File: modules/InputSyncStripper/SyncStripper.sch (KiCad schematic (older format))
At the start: 12 parts

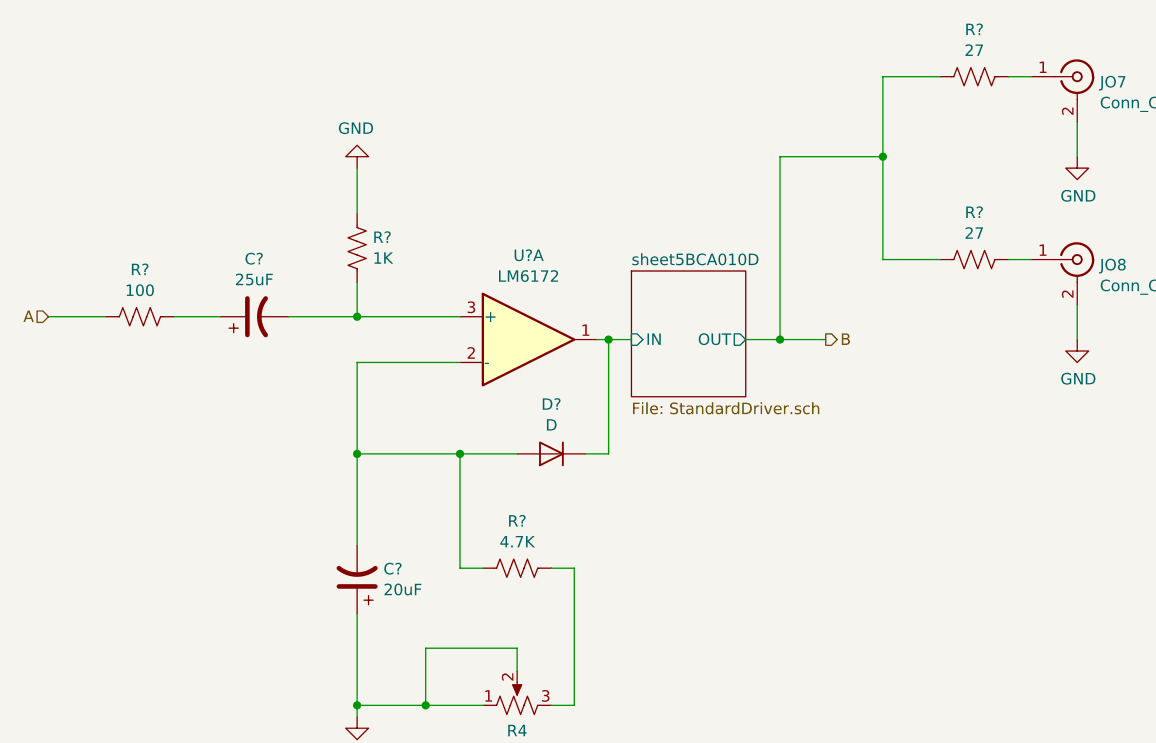
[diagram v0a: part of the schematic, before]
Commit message: fix some ERC issues; assign symbols
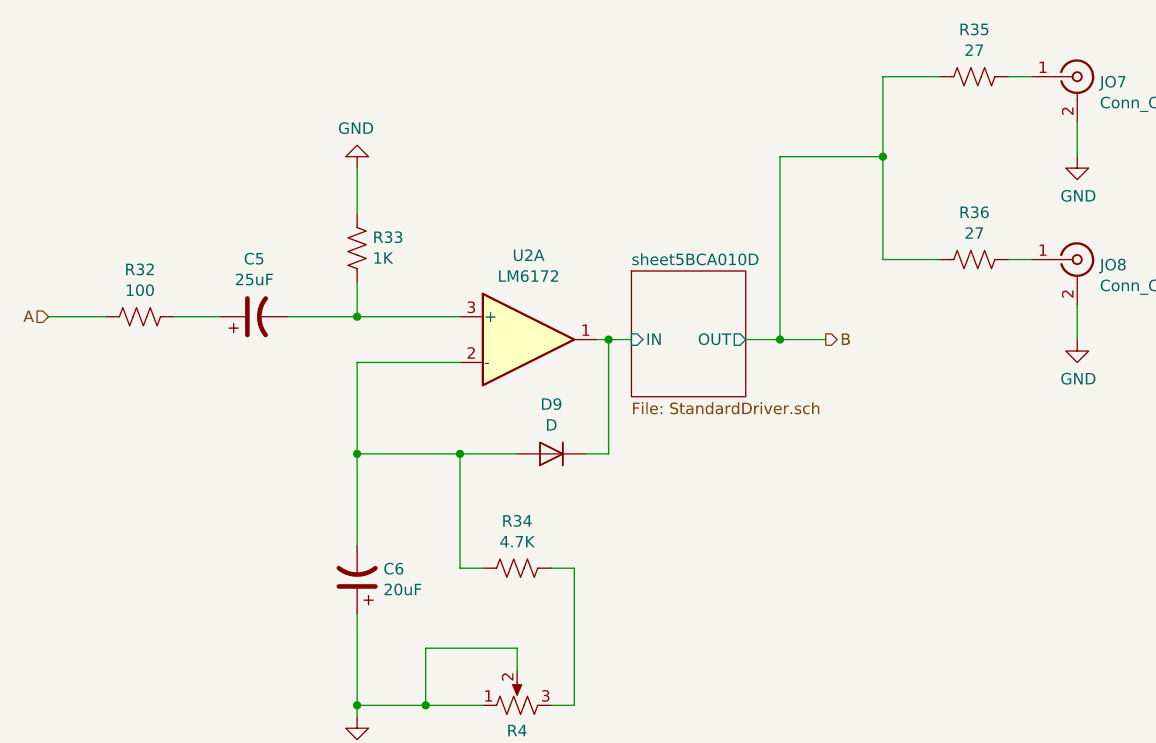
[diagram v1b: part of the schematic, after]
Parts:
- gave numbers to parts that had none: 9
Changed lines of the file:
@@
 EESchema Schematic File Version 4
-LIBS:SIP-cache
+LIBS:InputSyncStripper-cache
 EELAYER 26 0
 EELAYER END
@@
 B
 $Comp
-L Amplifier_Operational:LM6172 U?
+L Amplifier_Operational:LM6172 U2
 U 1 1 5BCA5CA5
 P 4550 3600
-F 0 "U?" H 4550 3967 50  0000 C CNN
+F 0 "U2" H 4550 3967 50  0000 C CNN
 F 1 "LM6172" H 4550 3876 50  0000 C CNN
 F 2 "" H 4550 3600 50  0001 C CNN
@@
 $EndComp
 $Comp
-L Device:R_US R?
+L Device:R_US R35
 U 1 1 5BCA026E
 P 6500 2450
-F 0 "R?" V 6295 2450 50  0000 C CNN
+F 0 "R35" V 6295 2450 50  0000 C CNN
 F 1 "27" V 6386 2450 50  0000 C CNN
 F 2 "" V 6540 2440 50  0001 C CNN
@@
 $EndComp
 $Comp
-L power:GND #PWR?
+L power:GND #PWR016
 U 1 1 5BCA04DE
 P 6950 2800
-F 0 "#PWR?" H 6950 2550 50  0001 C CNN
+F 0 "#PWR016" H 6950 2550 50  0001 C CNN
 F 1 "GND" H 6955 2627 50  0000 C CNN
 F 2 "" H 6950 2800 50  0001 C CNN
@@
 $EndComp
 $Comp
-L Device:R_US R?
+L Device:R_US R36
 U 1 1 5BCA0768
 P 6500 3250
-F 0 "R?" V 6295 3250 50  0000 C CNN
+F 0 "R36" V 6295 3250 50  0000 C CNN
 F 1 "27" V 6386 3250 50  0000 C CNN
 F 2 "" V 6540 3240 50  0001 C CNN
@@
 $EndComp
 $Comp
-L power:GND #PWR?
+L power:GND #PWR017
 U 1 1 5BCA076E
 P 6950 3600
-F 0 "#PWR?" H 6950 3350 50  0001 C CNN
+F 0 "#PWR017" H 6950 3350 50  0001 C CNN
 F 1 "GND" H 6955 3427 50  0000 C CNN
 F 2 "" H 6950 3600 50  0001 C CNN
@@
 $EndComp
 $Comp
-L Device:CP1 C?
+L Device:CP1 C6
 U 1 1 5BCA0CB3
 P 3800 4650
-F 0 "C?" H 3685 4604 50  0000 R CNN
+F 0 "C6" H 3685 4604 50  0000 R CNN
 F 1 "20uF" H 3685 4695 50  0000 R CNN
 F 2 "" H 3800 4650 50  0001 C CNN
@@
 $EndComp
 $Comp
-L Device:D D?
+L Device:D D9
 U 1 1 5BCA0DC4
 P 4650 4100
-F 0 "D?" H 4650 3884 50  0000 C CNN
+F 0 "D9" H 4650 3884 50  0000 C CNN
 F 1 "D" H 4650 3975 50  0000 C CNN
 F 2 "" H 4650 4100 50  0001 C CNN
@@
 	4900 3600 5000 3600
 $Comp
-L power:GND #PWR?
+L power:GND #PWR015
 U 1 1 5BCA11AF
 P 3800 5250
-F 0 "#PWR?" H 3800 5000 50  0001 C CNN
+F 0 "#PWR015" H 3800 5000 50  0001 C CNN
 F 1 "GND" H 3805 5077 50  0000 C CNN
 F 2 "" H 3800 5250 50  0001 C CNN
@@
 $EndComp
 $Comp
-L Device:R_US R?
+L Device:R_US R34
 U 1 1 5BCA123D
 P 4500 4600
-F 0 "R?" V 4295 4600 50  0000 C CNN
+F 0 "R34" V 4295 4600 50  0000 C CNN
 F 1 "4.7K" V 4386 4600 50  0000 C CNN
 F 2 "" V 4540 4590 50  0001 C CNN
@@
 	4100 5200 3800 5200
 $Comp
-L Device:CP1 C?
+L Device:CP1 C5
 U 1 1 5BCA29B1
 P 3350 3500
-F 0 "C?" V 3602 3500 50  0000 C CNN
+F 0 "C5" V 3602 3500 50  0000 C CNN
 F 1 "25uF" V 3511 3500 50  0000 C CNN
 F 2 "" H 3350 3500 50  0001 C CNN
@@
 $EndComp
 $Comp
-L Device:R_US R?
+L Device:R_US R32
 U 1 1 5BCA2A51
 P 2850 3500
-F 0 "R?" V 2645 3500 50  0000 C CNN
+F 0 "R32" V 2645 3500 50  0000 C CNN
 F 1 "100" V 2736 3500 50  0000 C CNN
 F 2 "" V 2890 3490 50  0001 C CNN
@@
 	3500 3500 3800 3500
 $Comp
-L Device:R_US R?
+L Device:R_US R33
 U 1 1 5BCA3DDE
 P 3800 3200
-F 0 "R?" H 3868 3246 50  0000 L CNN
+F 0 "R33" H 3868 3246 50  0000 L CNN
 F 1 "1K" H 3868 3155 50  0000 L CNN
 F 2 "" V 3840 3190 50  0001 C CNN
@@
 $EndComp
 $Comp
-L power:GND #PWR?
+L power:GND #PWR014
 U 1 1 5BCA3E47
 P 3800 2850
-F 0 "#PWR?" H 3800 2600 50  0001 C CNN
+F 0 "#PWR014" H 3800 2600 50  0001 C CNN
 F 1 "GND" H 3805 2677 50  0000 C CNN
 F 2 "" H 3800 2850 50  0001 C CNN

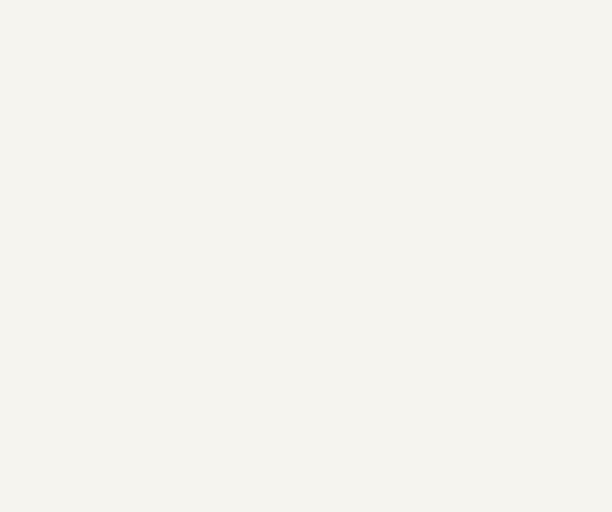
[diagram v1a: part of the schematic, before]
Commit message: added power pins for opamps and tied inputs of unused amp
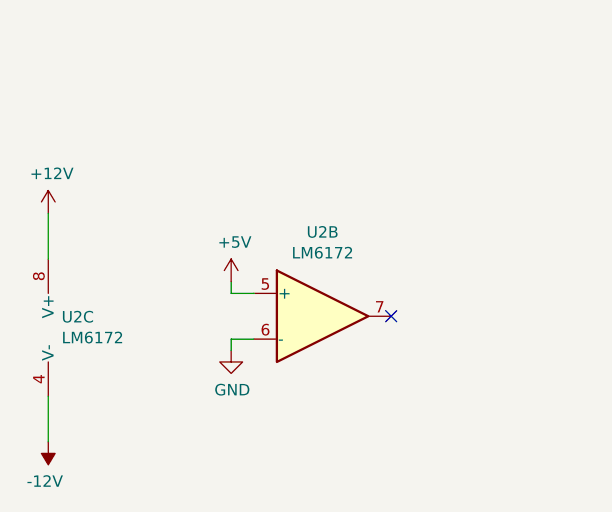
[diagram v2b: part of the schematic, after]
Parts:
- added unit 3 of U2
- added unit 2 of U2
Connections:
- net GND: now also U2.6 (-)
- new net +12V: U2.8 (V+)
- new net +5V: U2.5 (+)
- new net -12V: U2.4 (V-)
- no-connect marks 0 -> 1
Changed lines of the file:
@@
 Wire Wire Line
 	3800 3500 4250 3500
+$Comp
+L Amplifier_Operational:LM6172 U?
+U 3 1 5BCFD667
+P 1250 6700
+AR Path="/5BC7EA60/5BCFD667" Ref="U?"  Part="3"
+AR Path="/5BC9C4B4/5BCFD667" Ref="U2"  Part="3"
+F 0 "U2" H 1208 6746 50  0000 L CNN
+F 1 "LM6172" H 1208 6655 50  0000 L CNN
+F 2 "" H 1250 6700 50  0001 C CNN
+F 3 "http://www.ti.com/lit/ds/symlink/lm6172.pdf" H 1250 6700 50  0001 C CNN
+	3    1250 6700
+	1    0    0    -1
+$EndComp
+$Comp
+L power:+12V #PWR?
+U 1 1 5BCFD66E
+P 1150 6200
+AR Path="/5BC7EA60/5BCFD66E" Ref="#PWR?"  Part="1"
+AR Path="/5BC9C4B4/5BCFD66E" Ref="#PWR0112"  Part="1"
+F 0 "#PWR0112" H 1150 6050 50  0001 C CNN
+F 1 "+12V" H 1165 6373 50  0000 C CNN
+F 2 "" H 1150 6200 50  0001 C CNN
+F 3 "" H 1150 6200 50  0001 C CNN
+	1    1150 6200
+	1    0    0    -1
+$EndComp
+$Comp
+L power:-12V #PWR?
+U 1 1 5BCFD674
+P 1150 7200
+AR Path="/5BC7EA60/5BCFD674" Ref="#PWR?"  Part="1"
+AR Path="/5BC9C4B4/5BCFD674" Ref="#PWR0113"  Part="1"
+F 0 "#PWR0113" H 1150 7300 50  0001 C CNN
+F 1 "-12V" H 1165 7373 50  0000 C CNN
+F 2 "" H 1150 7200 50  0001 C CNN
+F 3 "" H 1150 7200 50  0001 C CNN
+	1    1150 7200
+	-1   0    0    1
+$EndComp
+Wire Wire Line
+	1150 7200 1150 7000
+Wire Wire Line
+	1150 6400 1150 6200
+$Comp
+L Amplifier_Operational:LM6172 U2
+U 2 1 5BD03947
+P 2350 6650
+F 0 "U2" H 2350 7017 50  0000 C CNN
+F 1 "LM6172" H 2350 6926 50  0000 C CNN
+F 2 "" H 2350 6650 50  0001 C CNN
+F 3 "http://www.ti.com/lit/ds/symlink/lm6172.pdf" H 2350 6650 50  0001 C CNN
+	2    2350 6650
+	1    0    0    -1
+$EndComp
+$Comp
+L power:GND #PWR0116
+U 1 1 5BD03A1E
+P 1950 6800
+F 0 "#PWR0116" H 1950 6550 50  0001 C CNN
+F 1 "GND" H 1955 6627 50  0000 C CNN
+F 2 "" H 1950 6800 50  0001 C CNN
+F 3 "" H 1950 6800 50  0001 C CNN
+	1    1950 6800
+	1    0    0    -1
+$EndComp
+$Comp
+L power:+5V #PWR0117
+U 1 1 5BD03A94
+P 1950 6500
+F 0 "#PWR0117" H 1950 6350 50  0001 C CNN
+F 1 "+5V" H 1965 6673 50  0000 C CNN
+F 2 "" H 1950 6500 50  0001 C CNN
+F 3 "" H 1950 6500 50  0001 C CNN
+	1    1950 6500
+	1    0    0    -1
+$EndComp
+Wire Wire Line
+	1950 6500 1950 6550
+Wire Wire Line
+	1950 6550 2050 6550
+Wire Wire Line
+	1950 6800 1950 6750
+Wire Wire Line
+	1950 6750 2050 6750
+NoConn ~ 2650 6650
 $EndSCHEMATC

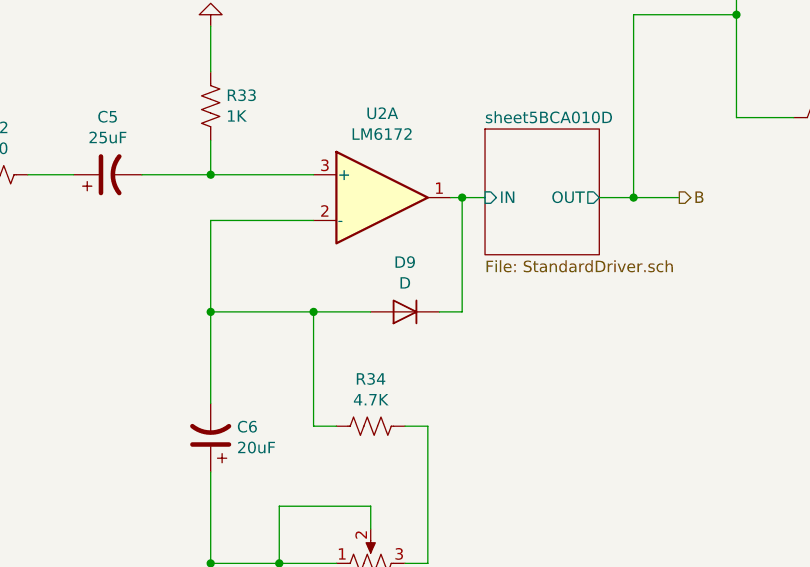
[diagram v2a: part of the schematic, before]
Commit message: Find and fix missing values
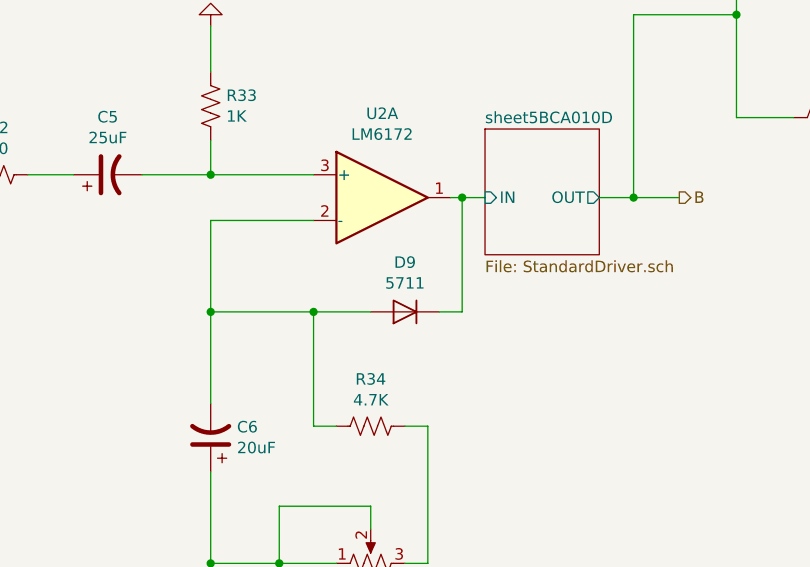
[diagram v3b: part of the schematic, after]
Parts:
- D9: value D -> 5711
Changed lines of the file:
@@
 P 4650 4100
 F 0 "D9" H 4650 3884 50  0000 C CNN
-F 1 "D" H 4650 3975 50  0000 C CNN
+F 1 "5711" H 4650 3975 50  0000 C CNN
 F 2 "" H 4650 4100 50  0001 C CNN
 F 3 "~" H 4650 4100 50  0001 C CNN

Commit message: building out footprints/BOM
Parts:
- C5: footprint (none) -> Capacitor_SMD:CP_Elec_6.3x5.4
- C6: footprint (none) -> Capacitor_SMD:CP_Elec_5x5.4
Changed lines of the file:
@@
 F 0 "C6" H 3685 4604 50  0000 R CNN
 F 1 "20uF" H 3685 4695 50  0000 R CNN
-F 2 "" H 3800 4650 50  0001 C CNN
+F 2 "Capacitor_SMD:CP_Elec_5x5.4" H 3800 4650 50  0001 C CNN
 F 3 "~" H 3800 4650 50  0001 C CNN
 	1    3800 4650
@@
 F 0 "C5" V 3602 3500 50  0000 C CNN
 F 1 "25uF" V 3511 3500 50  0000 C CNN
-F 2 "" H 3350 3500 50  0001 C CNN
+F 2 "Capacitor_SMD:CP_Elec_6.3x5.4" H 3350 3500 50  0001 C CNN
 F 3 "~" H 3350 3500 50  0001 C CNN
 	1    3350 3500
